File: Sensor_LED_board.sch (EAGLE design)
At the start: 22 parts, among them T1 2N2222

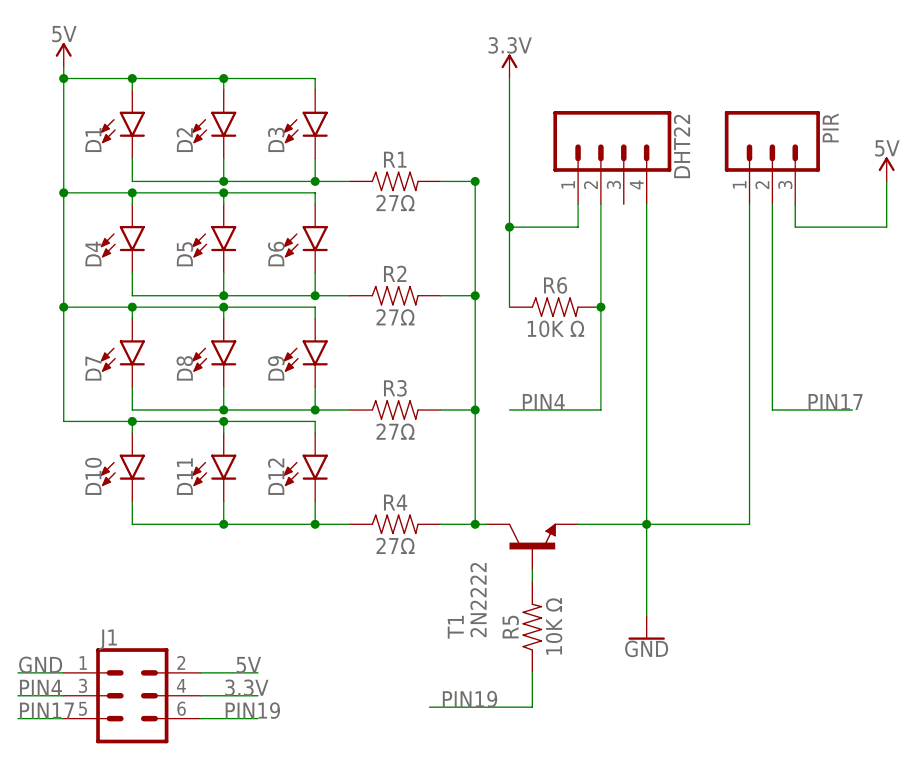
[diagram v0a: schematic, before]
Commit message: Put LED resistors in series, not parallel.
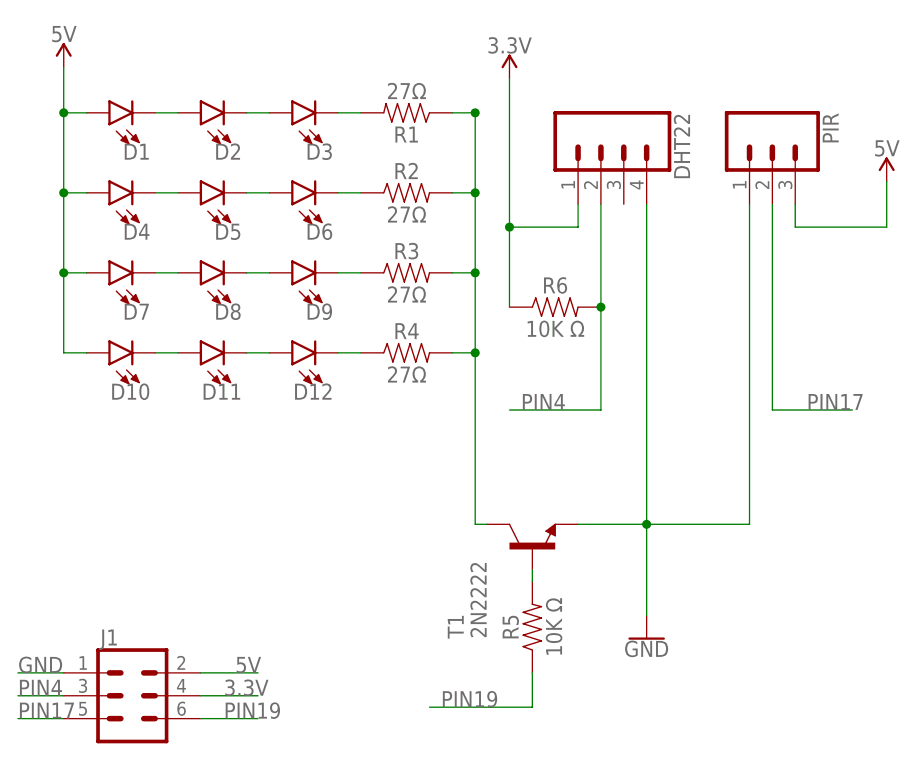
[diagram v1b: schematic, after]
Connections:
- new net N$10: D8.C, D9.A
- new net N$11: D11.C, D12.A
- new net N$12: D6.C, R2.1
- new net N$13: D9.C, R3.1
- new net N$14: D12.C, R4.1
- new net N$7: D2.C, D3.A
- new net N$8: D3.C, R1.2
- new net N$9: D5.C, D6.A
- net 5V: no longer D11.A, D12.A, D2.A, D3.A, D5.A, D6.A, D8.A, D9.A
- net N$1: now also D2.A; no longer D2.C, D3.C, R1.1
- net N$2: now also D5.A; no longer D5.C, D6.C, R2.1
- net N$3: now also D8.A; no longer D8.C, D9.C, R3.1
- net N$5: now also D11.A; no longer D11.C, D12.C, R4.1
- net N$6: now also R1.1; no longer R1.2
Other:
- moved on the sheet: D1, D10, D11, D12, D2, D3, D4, D5, D6, D7, D8, D9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
